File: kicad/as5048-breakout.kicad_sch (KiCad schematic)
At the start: 11 parts, among them J1 Conn_01x05, SW1 ADDR SELECT, U1 AS5048B

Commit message: fix: bom LCSC part no
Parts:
- C1: LCSC Part (none) -> C15850; LCSC_Part C15850 -> (none)
- C2: LCSC Part (none) -> C28233; LCSC_Part C28233 -> (none)
- R1, R2: LCSC Part (none) -> C25804
- SW1: LCSC Part (none) -> C54949; LCSC_Part C54949 -> (none)
- U1: LCSC Part (none) -> C2655184
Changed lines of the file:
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@@
 			)
 		)
-		(property "LCSC_Part" "C54949"
+		(property "LCSC Part" "C54949"
 			(at 106.68 67.31 0)
 			(effects
@@
 			)
 		)
+		(property "LCSC Part" "C25804"
+			(at 120.65 72.39 0)
+			(effects
+				(font
+					(size 1.27 1.27)
+				)
+				(hide yes)
+			)
+		)
 		(pin "1"
 		)
@@
 			)
 		)
-		(property "LCSC_Part" "C28233"
+		(property "LCSC Part" "C28233"
 			(at 175.26 66.04 0)
 			(effects
@@
 			)
 		)
+		(property "LCSC Part" "C2655184"
+			(at 153.67 82.55 0)
+			(effects
+				(font
+					(size 1.27 1.27)
+				)
+				(hide yes)
+			)
+		)
 		(pin "10"
 		)
@@
 			)
 		)
-		(property "LCSC_Part" "C15850"
+		(property "LCSC Part" "C15850"
 			(at 166.37 66.04 0)
 			(effects
@@
 			(at 127 72.39 0)
 			(effects
+				(font
+					(size 1.27 1.27)
+				)
+				(hide yes)
+			)
+		)
+		(property "LCSC Part" "C25804"
+			(at 127 72.39 0)
+			(effects

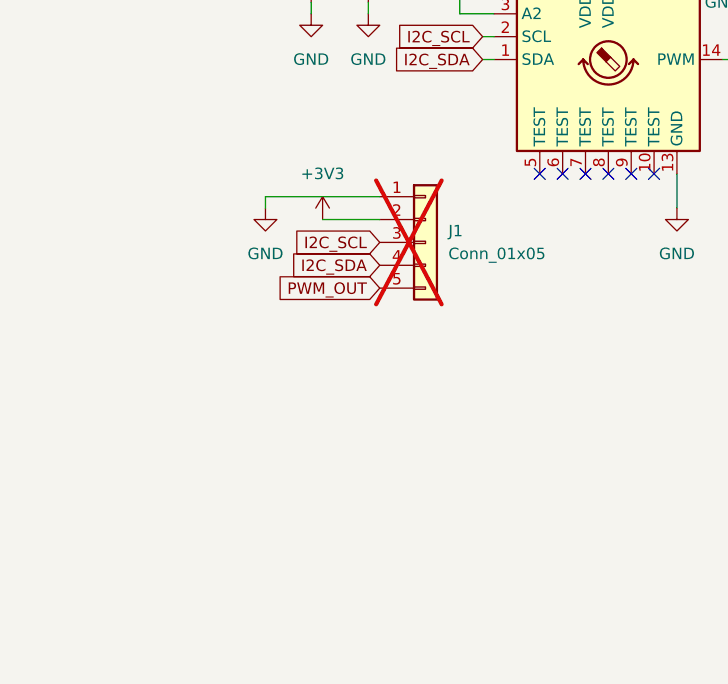
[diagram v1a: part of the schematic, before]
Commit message: feat: change pinheader to JST SH 1x4
with same pinouts as the Adafruit Qwiic or Stemma
connectors so that they could be used with their boards
(different pitch connectors used)
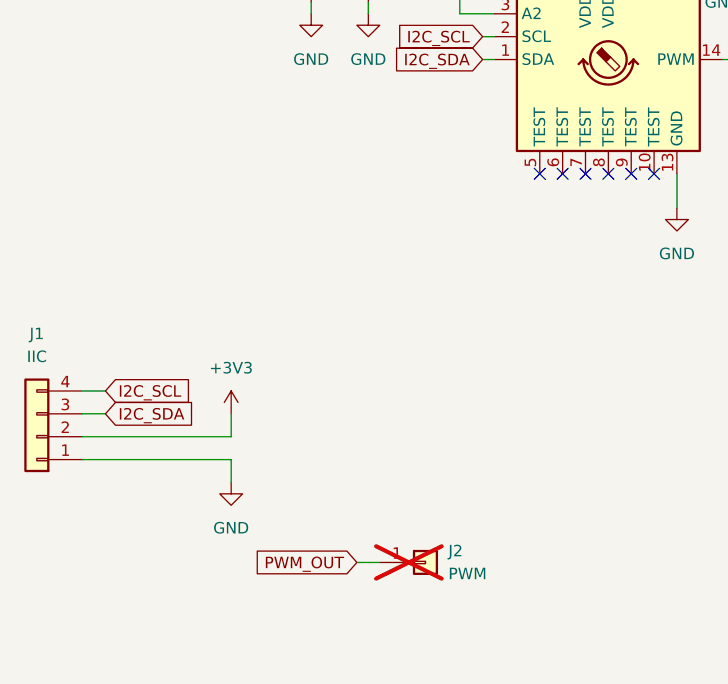
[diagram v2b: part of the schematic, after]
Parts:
- removed J1: Conn_01x05, Connector_PinHeader_2.54mm:PinHeader_1x05_P2.54mm_Vertical, symbol Connector_Generic:Conn_01x05
- added J1: IIC, Connector_JST:JST_SH_SM04B-SRSS-TB_1x04-1MP_P1.00mm_Horizontal, symbol Connector_Generic:Conn_01x04
- added J2: PWM, Connector_Wire:SolderWirePad_1x01_SMD_1x2mm, symbol Connector_Generic:Conn_01x01
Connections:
- net +3V3: now also J1.2 (Pin_2)
- net GND: now also J1.1 (Pin_1)
- net I2C_SCL: now also J1.4 (Pin_4)
- net I2C_SDA: now also J1.3 (Pin_3)
- net PWM_OUT: now also J2.1 (Pin_1)
